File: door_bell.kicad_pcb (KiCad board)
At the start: 4 copper layers, 68.6 x 68.6 mm, 75 parts, among them J1 8-10V AC/DC, J2 Speaker, J3 SWITCH1, J4 Door panel, J5 UART, J6 JTAG, J7 BOOT, J8 MicroSD, K1 HJR 1-2C, Q1 BC338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

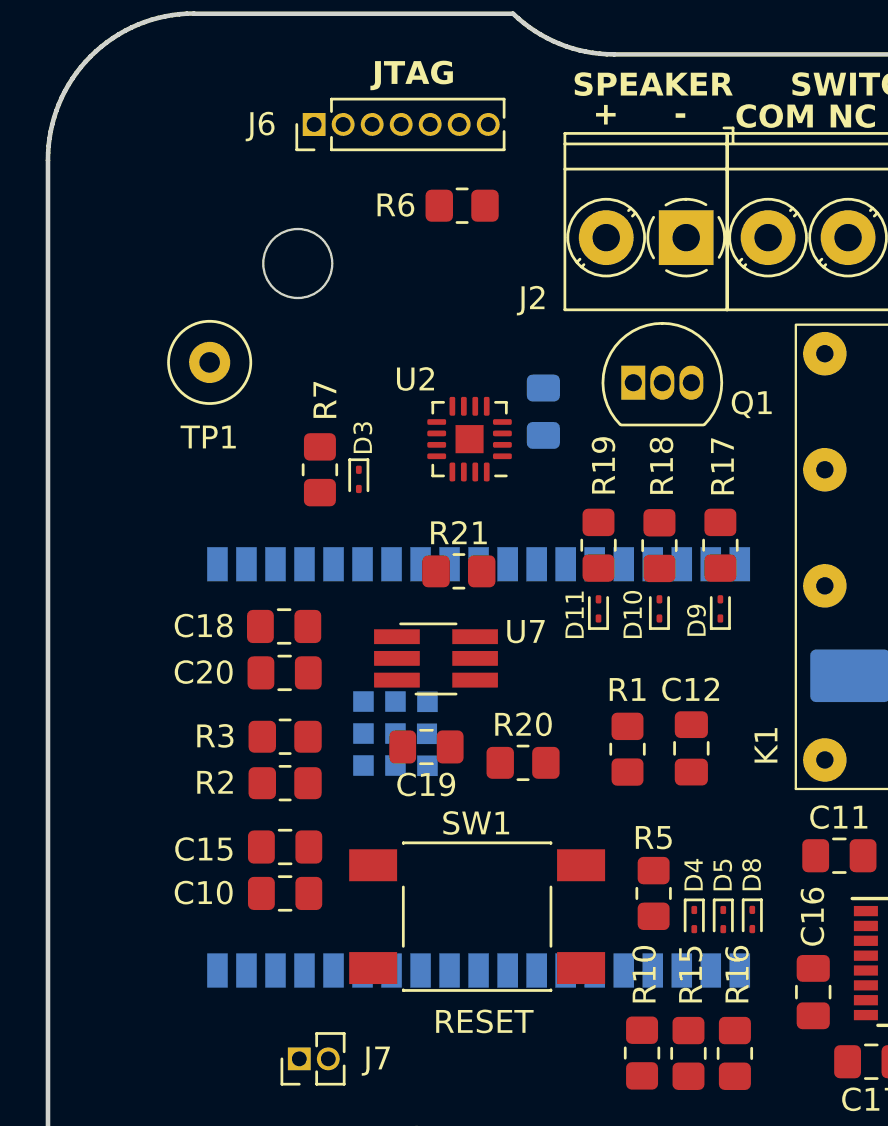
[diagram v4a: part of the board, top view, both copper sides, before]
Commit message: Update PCB with 3D model for ESP32
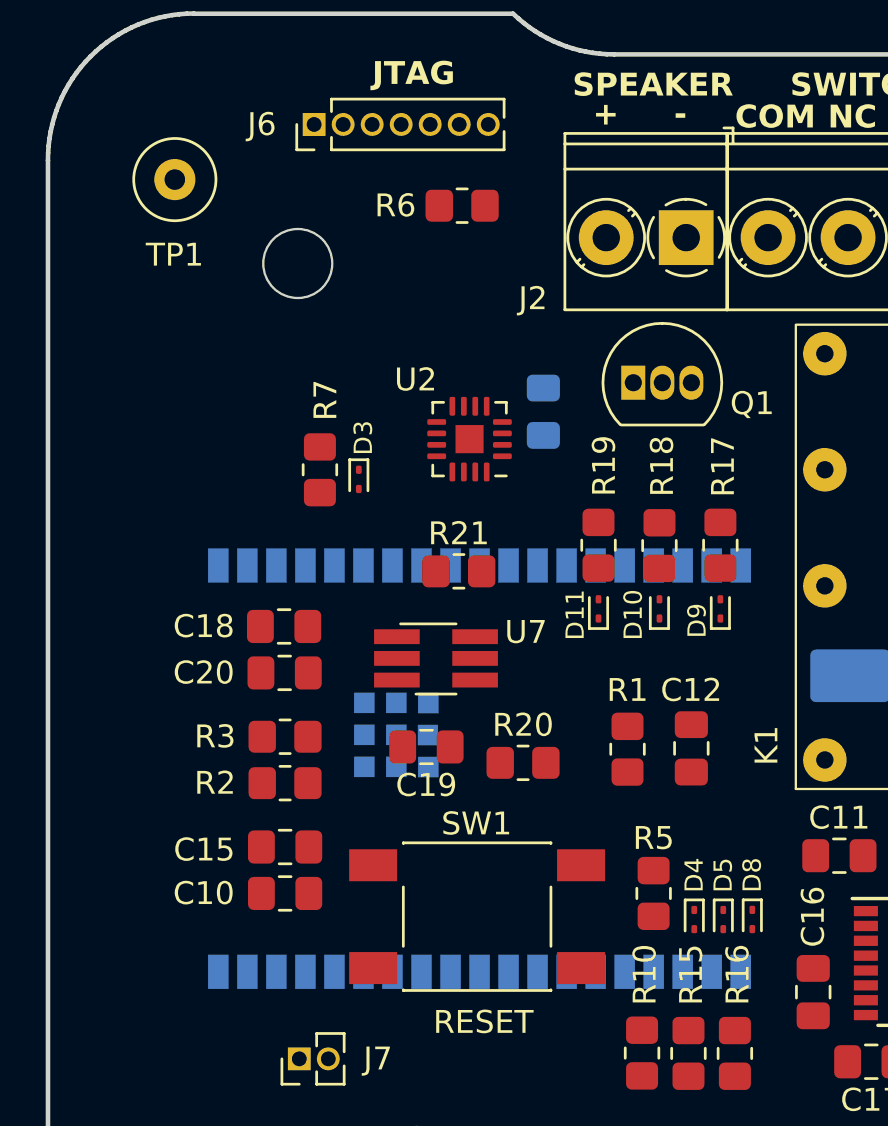
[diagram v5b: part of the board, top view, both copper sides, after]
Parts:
- moved TP1 8.14 mm to (110.5, 61.0)
- moved U6 0.07 mm to (112.4, 77.9)
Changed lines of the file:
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@@
   )
   (footprint "TestPoint:TestPoint_Loop_D3.50mm_Drill0.9mm_Beaded" (layer "F.Cu")
-    (at 112.014 68.961)
+    (at 110.49 60.96)
     (descr "wire loop with bead as test point, loop diameter2.6mm, hole diameter 0.9mm")
     (tags "test point wire loop bead")
@@
     )
   )
-  (footprint "Diode_SMD_espena:D_HDS20M_Rectifier" (layer "B.Cu")
-    (at 156.845 98.044 180)
-    (property "Sheetfile" "door_bell.kicad_sch")
-    (property "Sheetname" "")
-    (property "ki_description" "Diode bridge, +ve/AC/-ve/AC")
-    (property "ki_keywords" "rectifier ACDC")
-    (attr smd)
-    (fp_text reference "D1" (at -2.921 3.81 unlocked) (layer "B.SilkS")
-        (effects (font (size 1 1) (thickness 0.1)) (justify mirror))
-    )
-    (fp_text value "HDS20M" (at 0 -5.08 unlocked) (layer "B.Fab") hide
-        (effects (font (size 1 1) (thickness 0.15)) (justify mirror))
-    )
-    (fp_rect (start -4.064 2.794) (end 4.064 -2.794)
-      (stroke (width 0.1) (type default)) (fill none) (layer "B.SilkS"))
-    (pad "1" smd rect (at -2.794 1.27 180) (size 1.7 1.2) (layers "B.Cu" "B.Paste" "B.Mask")
-      (net 3 "+VDC") (pinfunction "+") (pintype "passive"))
-    (pad "2" smd rect (at -2.794 -1.27 180) (size 1.7 1.2) (layers "B.Cu" "B.Paste" "B.Mask")
-      (net 16 "Net-(J1-Pin_1)") (pintype "passive"))
-    (pad "3" smd rect (at 2.794 -1.27 180) (size 1.7 1.2) (layers "B.Cu" "B.Paste" "B.Mask")
-      (net 2 "GND") (pinfunction "-") (pintype "passive"))
-    (pad "4" smd rect (at 2.794 1.27 180) (size 1.7 1.2) (layers "B.Cu" "B.Paste" "B.Mask")
-      (net 17 "Net-(D1-Pad4)") (pintype "passive"))
-  )
   (footprint "RF_Module_espena:ESP32-WROVER-B" (layer "B.Cu")
-    (at 112.355 77.794)
+    (at 112.395 77.851)
     (property "Sheetfile" "door_bell.kicad_sch")
     (property "Sheetname" "")
@@
     (property "ki_keywords" "RF Radio ESP ESP32 Espressif onboard PCB antenna")
     (attr smd)
-    (fp_text reference "U6" (at 1.056 -1.848 unlocked) (layer "B.SilkS")
+    (fp_text reference "U6" (at 26.88 1.36 180 unlocked) (layer "B.SilkS")
         (effects (font (size 1 1) (thickness 0.1)) (justify mirror))
     )
-    (fp_text value "ESP32-WROVER-B" (at 11.83 14.17 180 unlocked) (layer "B.Fab") hide
+    (fp_text value "ESP32-WROVER-B" (at 11.83 14.17 180 unlocked) (layer "B.Fab")
         (effects (font (size 1 1) (thickness 0.15)) (justify mirror))
     )
@@
     (pad "38" smd rect (at 0 17.78) (size 0.9 1.5) (layers "B.Cu" "B.Paste" "B.Mask")
       (net 2 "GND") (pinfunction "GND3") (pintype "power_in"))
-    (group "" (id 046f0d2f-1e7f-433c-bdb8-199af8b64c65)
+    (group "" (id d28b5833-01b2-44e5-bfa8-1b6663d30801)
       (members
-        07d37848-149f-44b4-b889-3dbb3d414750
-        091c0386-7713-48f6-a0b3-a40950f467a5
-        34da606c-475b-44bf-9d6d-a165f729c5b0
-        85022c70-65da-445f-9b8f-54e1c380e3d5
-        8e18a39b-ebbc-463a-8ed8-0b9cff963434
-        b32860a6-973c-47b9-aa71-22181b90b957
-        d175da6d-a991-4428-90df-1ca2548bcb63
-        dad570a1-3dbc-412a-bf7f-855e7caa63dd
-        f50f94ab-922b-4dee-8610-49badb0c725e
+        01096084-b117-4760-bcad-1ed184e01e7a
+        043ba629-7c83-4f29-9c12-451167475172
+        177ac0b8-e1dc-46ad-a1a6-04d220800986
+        26835d36-484f-49ad-a684-60adf4fa769a
+        2881e41e-596a-4f30-86c8-74608ac9362e
+        392dbefb-27ed-47cf-918d-7efc9660f9d2
+        73994e06-2203-4091-860c-2b1362e78f62
+        783d1802-b37f-449c-b580-0fe83d3d4ce4
+        d5fc189a-4470-43e0-b1db-aedba2496214
       )
     )
+    (model ":KICAD_ROOT:libraries/snapeda/3dmodels/RF_Modules_snapeda/ESP32-WROVER-B.step"
+      (offset (xyz 8.25 8.85 0))
+      (scale (xyz 1 1 1))
+      (rotate (xyz -90 0 -90))
+    )
+  )
+  (footprint "Diode_SMD_espena:D_HDS20M_Rectifier" (layer "B.Cu")
+    (at 156.845 98.044 180)
+    (property "Sheetfile" "door_bell.kicad_sch")
+    (property "Sheetname" "")
+    (property "ki_description" "Diode bridge, +ve/AC/-ve/AC")
+    (property "ki_keywords" "rectifier ACDC")
+    (attr smd)
+    (fp_text reference "D1" (at -2.921 3.81 unlocked) (layer "B.SilkS")
+        (effects (font (size 1 1) (thickness 0.1)) (justify mirror))
+    )
+    (fp_text value "HDS20M" (at 0 -5.08 unlocked) (layer "B.Fab") hide
+        (effects (font (size 1 1) (thickness 0.15)) (justify mirror))
+    )
+    (fp_rect (start -4.064 2.794) (end 4.064 -2.794)
+      (stroke (width 0.1) (type default)) (fill none) (layer "B.SilkS"))
+    (pad "1" smd rect (at -2.794 1.27 180) (size 1.7 1.2) (layers "B.Cu" "B.Paste" "B.Mask")
+      (net 3 "+VDC") (pinfunction "+") (pintype "passive"))
+    (pad "2" smd rect (at -2.794 -1.27 180) (size 1.7 1.2) (layers "B.Cu" "B.Paste" "B.Mask")
+      (net 16 "Net-(J1-Pin_1)") (pintype "passive"))
+    (pad "3" smd rect (at 2.794 -1.27 180) (size 1.7 1.2) (layers "B.Cu" "B.Paste" "B.Mask")
+      (net 2 "GND") (pinfunction "-") (pintype "passive"))
+    (pad "4" smd rect (at 2.794 1.27 180) (size 1.7 1.2) (layers "B.Cu" "B.Paste" "B.Mask")
+      (net 17 "Net-(D1-Pad4)") (pintype "passive"))
   )
   (footprint "Battery:BatteryHolder_Keystone_1058_1x2032" (layer "B.Cu")

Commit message: Adjust layout
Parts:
- moved R5 4.04 mm to (134.4, 89.4), turned to 0 degrees
- moved U2 2.74 mm to (123.0, 69.6), turned to 0 degrees
- moved C18 2.05 mm to (117.3, 80.5)
- moved C20 2.05 mm to (117.3, 82.5)
- moved J2 2.03 mm to (134.9, 63.4)
- moved J3 2.03 mm to (145.5, 63.4)
- moved C10 2.03 mm to (117.3, 92.2)
- moved C15 2.03 mm to (117.3, 90.2)
- moved R2 2.03 mm to (117.3, 87.4)
- moved R3 2.03 mm to (117.3, 85.3)
- moved SW1 2.01 mm to (125.7, 93.2)
- moved Q1 1.78 mm to (132.3, 69.8)
- moved U7 1.30 mm to (123.2, 81.7)
- moved C4 1.15 mm to (149.4, 73.2)
- moved TP1 1.14 mm to (111.0, 59.9)
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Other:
- outline, holes or cut-outs redrawn
- board text added: "B.OPT"
